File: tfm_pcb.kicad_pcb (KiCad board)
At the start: 2 copper layers, 73 x 55 mm, 74 parts, among them J1 Conn_01x02_MountingPin, J2 USB_B_Micro, J20 Conn_01x01_Socket, J21 Conn_01x01_Socket, J22 Conn_01x01_Socket, J23 Conn_01x01_Socket, J24 Conn_01x01_Socket, J3 Mounting Pin, U1 ESP32-S3-WROOM-2, U2 MCP73871-2CC, U3 ADS1292IPBS, U4 LSM6DS3, U5 USBLC6-2SC6, U6 XC6220B331MR, U7 USBLC6-2SC6

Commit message: Cambios envío a Roberto 06-09
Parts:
- removed 3.3VA, DRDY: Conn_01x01_Pin, TestPoint:TestPoint_Pad_D1.0mm
- added J14: Conn_01x01_Pin, TestPoint:TestPoint_Pad_D1.0mm, F.Cu at (142.3, 86.4)
- moved C7 3.45 mm to (151.8, 80.5)
- moved R4 1.35 mm to (110.9, 89.9)
- moved D2 1.05 mm to (107.0, 89.9)
- moved R3 0.85 mm to (111.2, 83.0)
- moved J4 0.76 mm to (132.3, 94.6)
- moved C23 0.60 mm to (133.0, 92.1)
- moved C6 0.60 mm to (153.5, 80.5)
- moved D1 0.60 mm to (107.0, 83.0)
- renumbered VREF to J12, GNDA to J13, I1N to J15, I1P to J16, I2N to J17, I2P to J18, IRLD to J19, 3.3V to J4, VBAT to J5, GND to J6, BOOT to S1, ENABLE to S2
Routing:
- net /DRDY: track 24.5 -> 20.0 mm, vias 2 -> 0
- net GNDA: track 7.33 -> 3.45 mm, vias 15 -> 35
- net +5V: track 99.2 -> 96.5 mm
- net Net-(J17-Pin_1): track 9.18 -> 7.86 mm
- net Net-(U2-STAT1/~{LBO}): track 4.71 -> 5.96 mm
- net +3.3VA: track 57.8 -> 58.9 mm
- net /VBAT: track 21.3 -> 22.0 mm
- net /MISO: track 20.2 -> 19.5 mm
- net GND: vias 27 -> 49

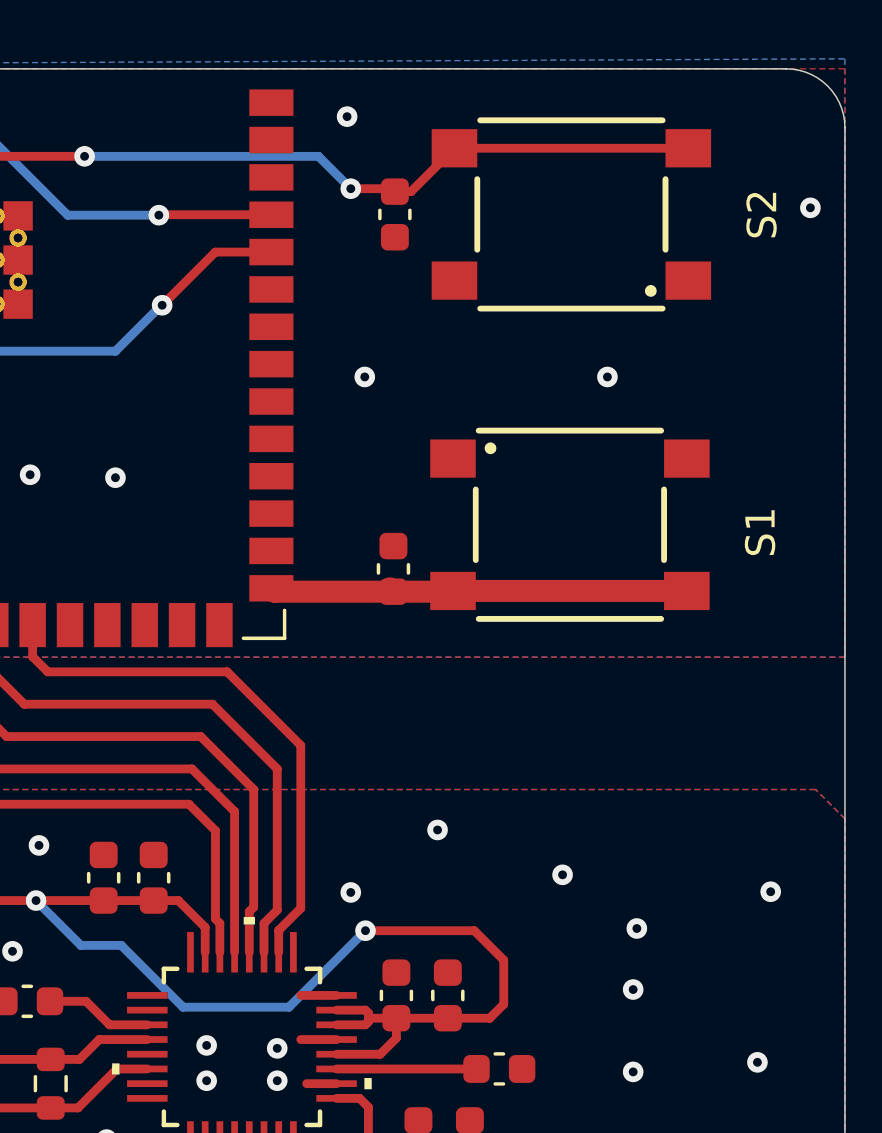
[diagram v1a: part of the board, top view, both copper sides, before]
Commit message: desactivo integracion git
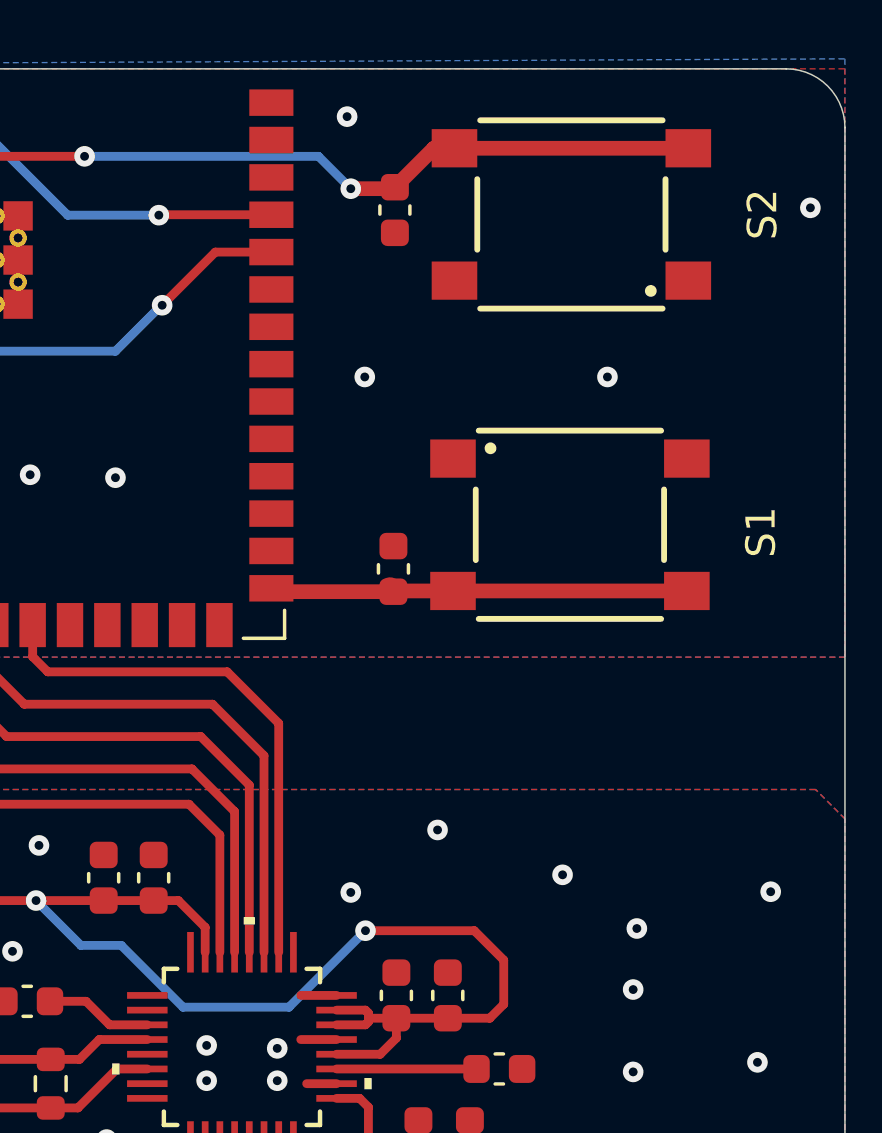
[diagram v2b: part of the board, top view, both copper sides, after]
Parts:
- moved C1 0.15 mm to (161.7, 57.8)
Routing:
- net /CS: track 18.8 -> 18.2 mm
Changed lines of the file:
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@@
 		(capping no)
 		(filling no)
+		(grid_origin 155.5 80.8)
 		(pcbplotparams
 			(layerselection 0x00000000_00000000_55555555_5755f5ff)
@@
 	(footprint "Capacitor_SMD:C_0603_1608Metric"
 		(layer "F.Cu")
-		(at 161.7 57.95 90)
+		(at 161.7 57.8 90)
 		(descr "Capacitor SMD 0603 (1608 Metric), square (rectangular) end terminal, IPC-7351 nominal, (Body size source: IPC-SM-782 page 76, https://www.pcb-3d.com/wordpress/wp-content/uploads/ipc-sm-782a_amendment_1_and_2.pdf), generated with kicad-footprint-generator")
 		(tags "capacitor")
@@
 	)
 	(segment
+		(start 161.65 57.075)
+		(end 161.7 57.025)
+		(width 0.3)
+		(layer "F.Cu")
+		(net "Net-(U1-EN)")
+	)
+	(segment
 		(start 161.6 57.075)
 		(end 161.7 57.175)
@@
 	)
 	(segment
-		(start 162.25 57.175)
-		(end 163.725 55.7)
-		(width 0.3)
+		(start 160.2 57.075)
+		(end 161.65 57.075)
+		(width 0.5)
+		(layer "F.Cu")
+		(net "Net-(U1-EN)")
+	)
+	(segment
+		(start 163.725 55.7)
+		(end 163.025 55.7)
+		(width 0.5)
 		(layer "F.Cu")
 		(net "Net-(U1-EN)")
@@
 	)
 	(segment
-		(start 133.825 58.5)
-		(end 137.1 58.5)
-		(width 0.3)
+		(start 163.025 55.7)
+		(end 161.7 57.025)
+		(width 0.5)
 		(layer "F.Cu")
 		(net "Net-(U1-EN)")
 	)
 	(segment
-		(start 163.725 55.7)
-		(end 171.675 55.7)
-		(width 0.3)
+		(start 171.675 55.7)
+		(end 163.725 55.7)
+		(width 0.5)
 		(layer "F.Cu")
 		(net "Net-(U1-EN)")
 	)
 	(segment
-		(start 161.7 57.175)
-		(end 162.25 57.175)
+		(start 133.825 58.5)
+		(end 137.1 58.5)
 		(width 0.3)
 		(layer "F.Cu")
@@
 	)
 	(segment
-		(start 163.6 55.7)
-		(end 163.725 55.7)
-		(width 0.75)
-		(layer "F.Cu")
-		(net "Net-(U1-EN)")
-	)
-	(segment
 		(start 138.91 56.69)
 		(end 140 56.69)
@@
 	)
 	(segment
-		(start 160.2 57.075)
-		(end 161.6 57.075)
+		(start 160.25 57.025)
+		(end 160.2 57.075)
 		(width 0.3)
 		(layer "F.Cu")
@@
 	)
 	(segment
+		(start 110.4 73.1)
+		(end 111.15 72.35)
+		(width 0.3)
+		(layer "F.Cu")
+		(net "Net-(J2-D-)")
+	)
+	(segment
+		(start 113.85 72.35)
+		(end 114.1 72.6)
+		(width 0.3)
+		(layer "F.Cu")
+		(net "Net-(J2-D-)")
+	)
+	(segment
+		(start 114.1 72.6)
+		(end 116.6125 72.6)
+		(width 0.3)
+		(layer "F.Cu")
+		(net "Net-(J2-D-)")
+	)
+	(segment
+		(start 111.15 72.35)
+		(end 113.85 72.35)
+		(width 0.3)
+		(layer "F.Cu")
+		(net "Net-(J2-D-)")
+	)
+	(segment
+		(start 108.7 73.1)
+		(end 110.4 73.1)
+		(width 0.3)
+		(layer "F.Cu")
+		(net "Net-(J2-D-)")
+	)
+	(segment
+		(start 114.1 74.5)
+		(end 113.8 74.8)
+		(width 0.3)
+		(layer "F.Cu")
+		(net "Net-(J2-D+)")
+	)
+	(segment
+		(start 111.2 74.8)
+		(end 110.15 73.75)
+		(width 0.3)
+		(layer "F.Cu")
+		(net "Net-(J2-D+)")
+	)
+	(segment
+		(start 113.8 74.8)
+		(end 111.2 74.8)
+		(width 0.3)
+		(layer "F.Cu")
+		(net "Net-(J2-D+)")
+	)
+	(segment
+		(start 110.15 73.75)
+		(end 108.7 73.75)
+		(width 0.3)
+		(layer "F.Cu")
+		(net "Net-(J2-D+)")
+	)
+	(segment
+		(start 116.6125 74.5)
+		(end 114.1 74.5)
+		(width 0.3)
+		(layer "F.Cu")
+		(net "Net-(J2-D+)")
+	)
+	(segment
 		(start 115.45 86.25)
 		(end 114.7 87)
@@
 	)
 	(segment
-		(start 161.65 70.775)
-		(end 163.65 70.775)
-		(width 0.75)
+		(start 171.625 70.75)
+		(end 161.675 70.75)
+		(width 0.5)
 		(layer "F.Cu")
 		(net "/BOOT")
@@
 		(start 157.615 70.775)
 		(end 157.5 70.66)
-		(width 0.75)
-		(layer "F.Cu")
-		(net "/BOOT")
-	)
-	(segment
-		(start 163.675 70.75)
-		(end 171.625 70.75)
-		(width 0.75)
+		(width 0.5)
 		(layer "F.Cu")
 		(net "/BOOT")
@@
 		(start 161.65 70.775)
 		(end 157.615 70.775)
-		(width 0.75)
+		(width 0.5)
+		(layer "F.Cu")
+		(net "/BOOT")
+	)
+	(segment
+		(start 161.675 70.75)
+		(end 161.65 70.775)
+		(width 0.5)
 		(layer "F.Cu")
 		(net "/BOOT")
@@
 	)
 	(segment
-		(start 155.6 78.9)
-		(end 154.7 78)
-		(width 0.3)
-		(layer "F.Cu")
-		(net "/DRDY")
-	)
-	(segment
 		(start 144.305 74.605)
 		(end 144.305 71.91)
@@
 	)
 	(segment
-		(start 147.7 78)
-		(end 144.305 74.605)
-		(width 0.3)
-		(layer "F.Cu")
-		(net "/DRDY")
-	)
-	(segment
-		(start 155.6 81.9)
-		(end 155.6 78.9)
+		(start 155.749999 83.033352)
+		(end 155.749999 79.049999)
 		(width 0.3)
 		(layer "F.Cu")
@@
 	)
 	(segment
-		(start 155.749999 82.049999)
-		(end 155.6 81.9)
+		(start 147.7 78)
+		(end 144.305 74.605)
 		(width 0.3)
 		(layer "F.Cu")
@@
 	)
 	(segment
-		(start 155.749999 83.033352)
-		(end 155.749999 82.049999)
+		(start 155.749999 79.049999)
+		(end 154.7 78)
 		(width 0.3)
 		(layer "F.Cu")
@@
 	)
 	(segment
-		(start 156.9 81.5)
-		(end 156.9 77.5)
-		(width 0.3)
-		(layer "F.Cu")
-		(net "/SCK")
-	)
-	(segment
-		(start 156.9 77.5)
-		(end 155.1 75.7)
-		(width 0.3)
-		(layer "F.Cu")
-		(net "/SCK")
-	)
-	(segment
 		(start 156.75 83.033352)
-		(end 156.75 81.65)
+		(end 156.75 77.35)
 		(width 0.3)
 		(layer "F.Cu")
@@
 	)
 	(segment
-		(start 148.5 75.7)
-		(end 146.845 74.045)
+		(start 156.75 77.35)
+		(end 155.1 75.7)
 		(width 0.3)
 		(layer "F.Cu")
@@
 	)
 	(segment
-		(start 156.75 81.65)
-		(end 156.9 81.5)
-		(width 0.3)
-		(layer "F.Cu")
-		(net "/SCK")
-	)
-	(segment
 		(start 155.1 75.7)
 		(end 148.5 75.7)
@@
 	)
 	(segment
-		(start 157.7 81.6)
-		(end 157.7 76.8)
-		(width 0.3)
-		(layer "F.Cu")
-		(net "/MOSI")
-	)
-	(segment
-		(start 157.250001 83.033352)
-		(end 157.250001 82.049999)
+		(start 148.5 75.7)
+		(end 146.845 74.045)
 		(width 0.3)
 		(layer "F.Cu")
-		(net "/MOSI")
+		(net "/SCK")
 	)
 	(segment
@@
 	)
 	(segment
-		(start 155.5 74.6)
-		(end 149.1 74.6)
-		(width 0.3)
-		(layer "F.Cu")
-		(net "/MOSI")
-	)
-	(segment
-		(start 157.250001 82.049999)
-		(end 157.7 81.6)
+		(start 157.250001 76.350001)
+		(end 155.5 74.6)
 		(width 0.3)
 		(layer "F.Cu")
@@
 	)
 	(segment
-		(start 157.7 76.8)
-		(end 155.5 74.6)
+		(start 157.250001 83.033352)
+		(end 157.250001 76.350001)
 		(width 0.3)
 		(layer "F.Cu")
@@
 	)
 	(segment
-		(start 158.5 81.53781)
-		(end 157.75 82.28781)
-		(width 0.3)
-		(layer "F.Cu")
-		(net "/CS")
-	)
-	(segment
-		(start 157.75 82.28781)
-		(end 157.75 83.033352)
-		(width 0.3)
-		(layer "F.Cu")
-		(net "/CS")
-	)
-	(segment
-		(start 149.9 73.5)
-		(end 156 73.5)
+		(start 155.5 74.6)
+		(end 149.1 74.6)
 		(width 0.3)
 		(layer "F.Cu")
-		(net "/CS")
+		(net "/MOSI")
 	)
 	(segment
@@
 	(segment
 		(start 156 73.5)
-		(end 158.5 76)
+		(end 157.75 75.25)
 		(width 0.3)
 		(layer "F.Cu")
@@
 	)
 	(segment
-		(start 158.5 76)
-		(end 158.5 81.53781)
+		(start 157.75 75.25)
+		(end 157.75 83.033352)
 		(width 0.3)
 		(layer "F.Cu")
@@
 	)
 	(segment
-		(start 114.1 74.5)
-		(end 113.8 74.8)
-		(width 0.3)
-		(layer "F.Cu")
-		(net "Net-(J2-D+)")
-	)
-	(segment
-		(start 111.2 74.8)
-		(end 110.15 73.75)
-		(width 0.3)
-		(layer "F.Cu")
-		(net "Net-(J2-D+)")
-	)
-	(segment
-		(start 113.8 74.8)
-		(end 111.2 74.8)
-		(width 0.3)
-		(layer "F.Cu")
-		(net "Net-(J2-D+)")
-	)
-	(segment
-		(start 110.15 73.75)
-		(end 108.7 73.75)
-		(width 0.3)
-		(layer "F.Cu")
-		(net "Net-(J2-D+)")
-	)
-	(segment
-		(start 116.6125 74.5)
-		(end 114.1 74.5)
-		(width 0.3)
-		(layer "F.Cu")
-		(net "Net-(J2-D+)")
-	)
-	(segment
-		(start 110.4 73.1)
-		(end 111.15 72.35)
-		(width 0.3)
-		(layer "F.Cu")
-		(net "Net-(J2-D-)")
-	)
-	(segment
-		(start 113.85 72.35)
-		(end 114.1 72.6)
-		(width 0.3)
-		(layer "F.Cu")
-		(net "Net-(J2-D-)")
-	)
-	(segment
-		(start 114.1 72.6)
-		(end 116.6125 72.6)
-		(width 0.3)
-		(layer "F.Cu")
-		(net "Net-(J2-D-)")
-	)
-	(segment
-		(start 111.15 72.35)
-		(end 113.85 72.35)
-		(width 0.3)
-		(layer "F.Cu")
-		(net "Net-(J2-D-)")
-	)
-	(segment
-		(start 108.7 73.1)
-		(end 110.4 73.1)
+		(start 149.9 73.5)
+		(end 156 73.5)
 		(width 0.3)
 		(layer "F.Cu")
-		(net "Net-(J2-D-)")
+		(net "/CS")
 	)
 	(zone

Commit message: cambios
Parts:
- removed J14, J4: Conn_01x01_Pin, TestPoint:TestPoint_Pad_D1.0mm
- removed R15: 0, Resistor_SMD:R_0603_1608Metric
- FB1: value FerriteBead -> (none); footprint Resistor_SMD:R_0603_1608Metric -> Inductor_SMD:L_0603_1608Metric
- moved FB1 5.40 mm to (139.4, 87.2), turned to 0 degrees
- moved C23 4.88 mm to (135.8, 88.1), turned to 90 degrees
- moved C21 0.59 mm to (133.4, 88.1), turned to 90 degrees
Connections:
- C10 pad 2: GNDA -> GND
- C11 pad 2: GNDA -> GND
- C12 pad 1: GNDA -> GND
- C13 pad 1: GNDA -> GND
- C6 pad 1: GNDA -> GND
- C7 pad 1: GNDA -> GND
- C8 pad 2: GNDA -> GND
- C9 pad 1: GNDA -> GND
- FB1 pad 1: +3.3VA -> +3.3V
- FB1 pad 2: +3.3V -> +3.3VA
- J13 pad 1: GNDA -> GND
- J20 pad 1: GNDA -> GND
- J21 pad 1: GNDA -> GND
- J22 pad 1: GNDA -> GND
- J23 pad 1: GNDA -> GND
- J24 pad 1: GNDA -> GND
- U3 pad 10: GNDA -> GND
- U3 pad 13: GNDA -> GND
- U3 pad 16: GNDA -> GND
- U3 pad 24: GNDA -> GND
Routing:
- net +3.3VA: track 58.9 -> 49.6 mm
- net +3.3V: track 92.4 -> 87.0 mm
- net GND: track 8.87 -> 12.5 mm, vias 49 -> 95
- net GNDA: track 3.45 -> 0.00 mm, vias 35 -> 0
- removed copper zone on B.Cu, net GNDA
- removed copper zone on F.Cu, net GNDA
